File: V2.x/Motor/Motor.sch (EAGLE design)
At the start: 48 parts, among them IC1 Atmega 328-P, IC2 MCP2515, IC3 LM340MP-05, Q1 8MHz, Q2 16MHz

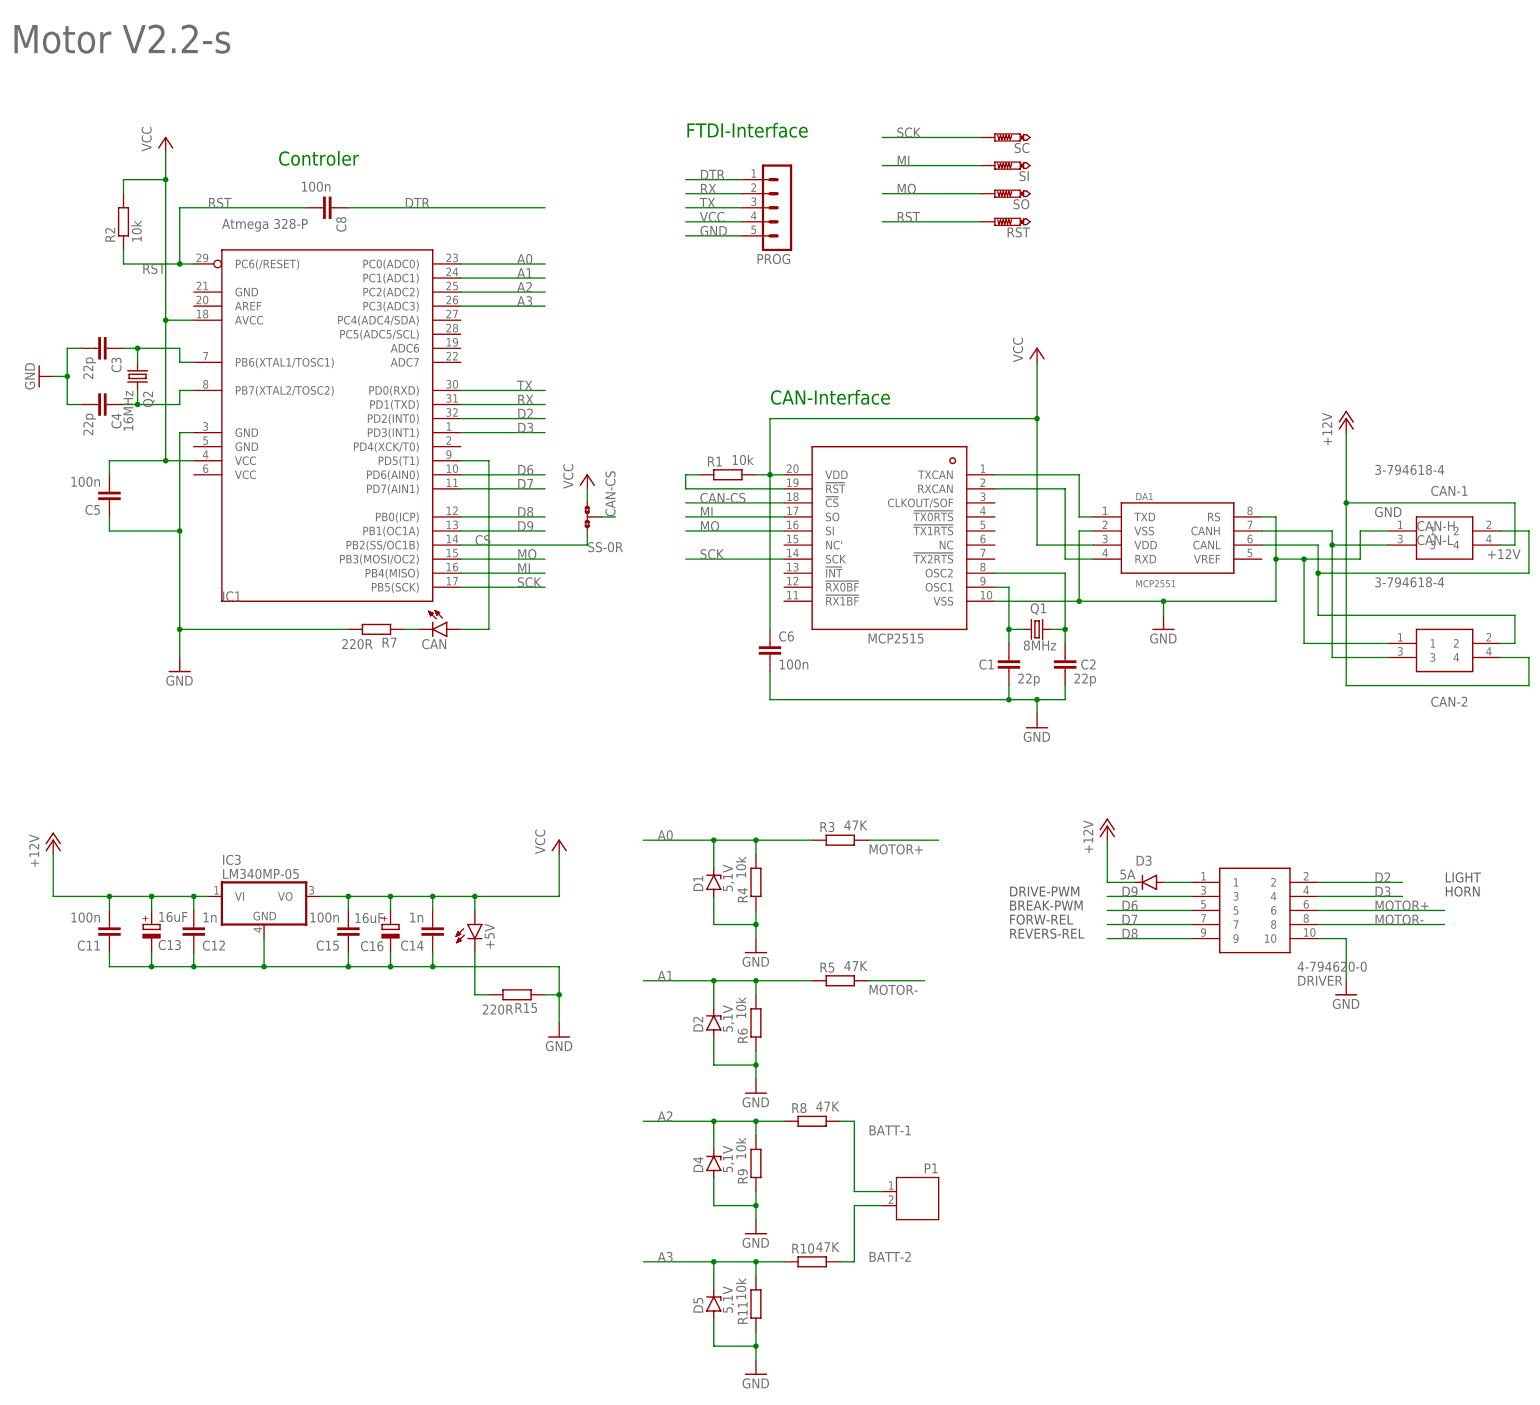
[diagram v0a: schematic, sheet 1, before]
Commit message: added Loco-CAN icon to motor, servo and switch boards
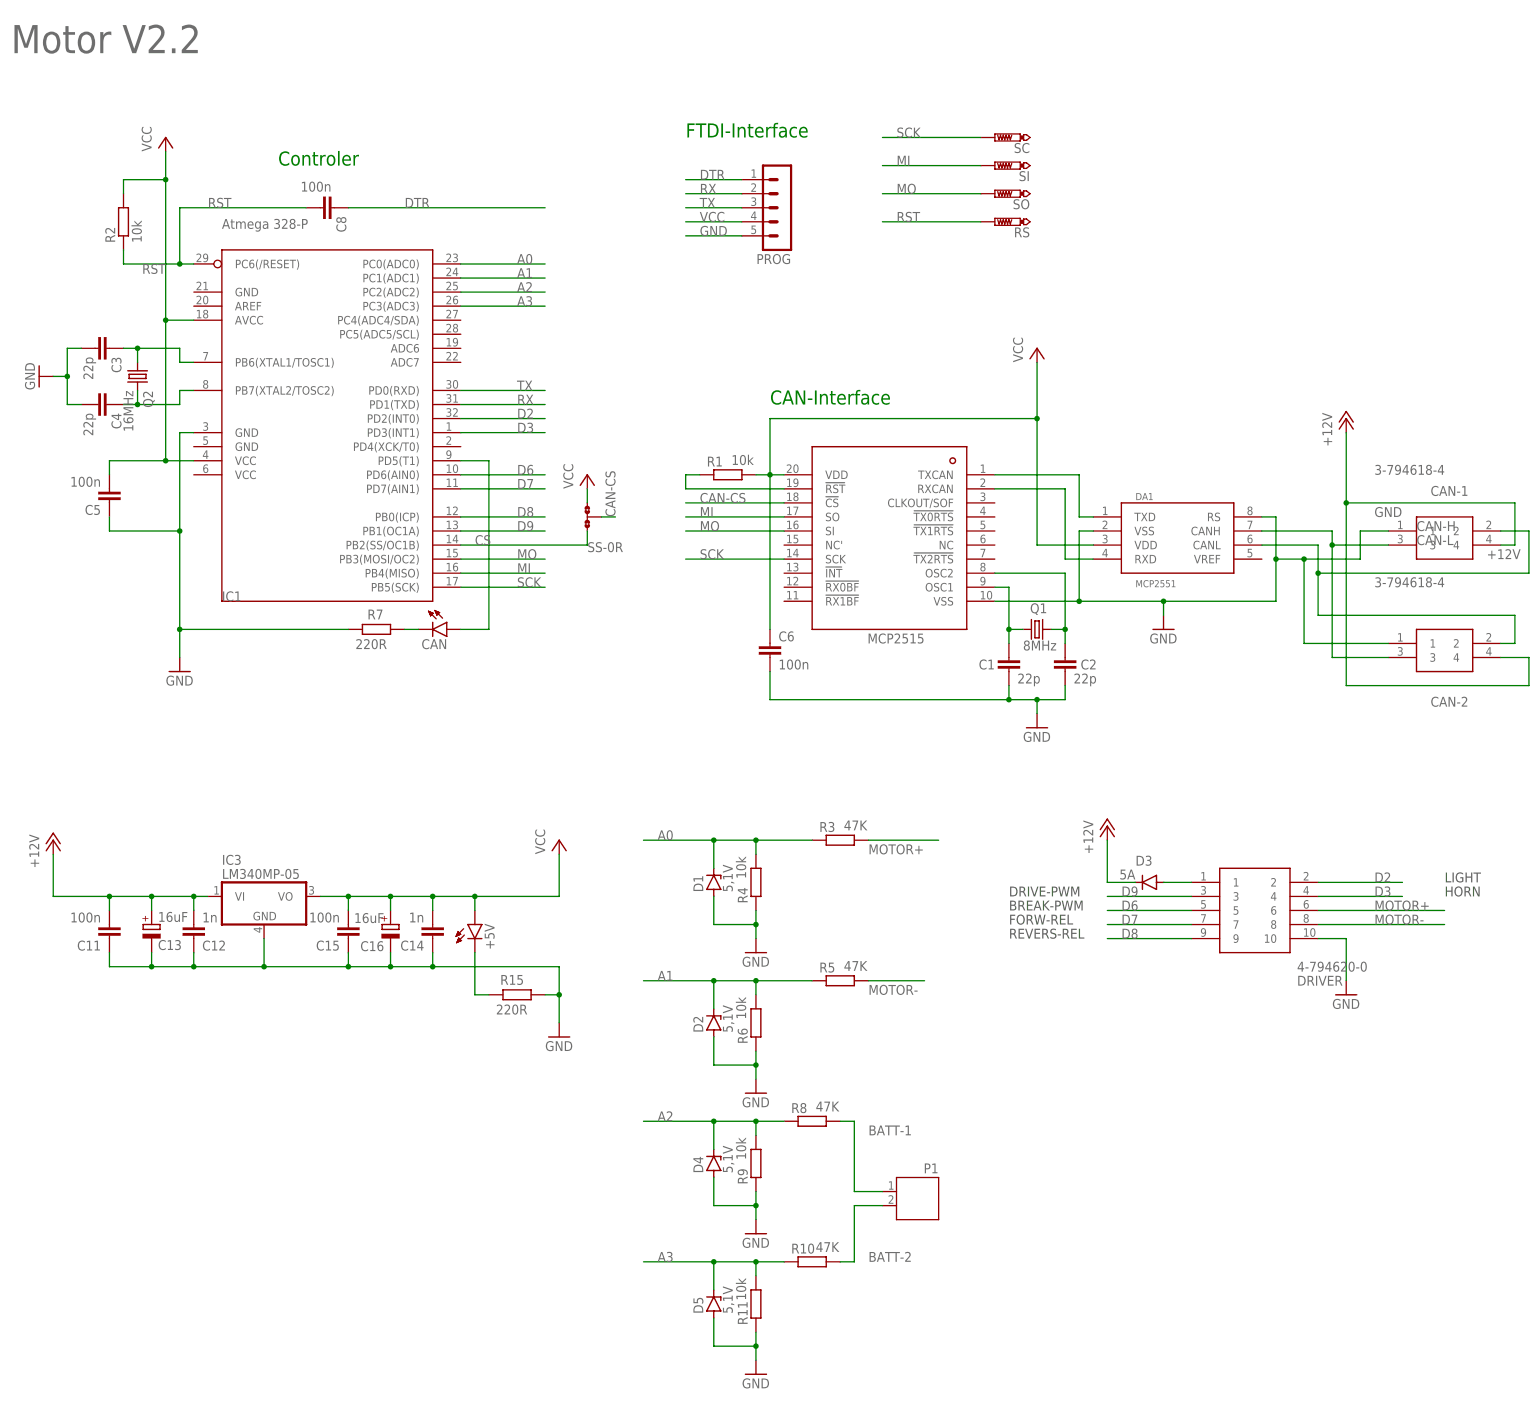
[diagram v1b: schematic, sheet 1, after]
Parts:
- renumbered RST to RS
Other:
- note added: "Motor V2.2"
- note removed: "Motor V2.2-s"
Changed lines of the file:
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@@
 <part name="SS" library="jump-0r-smd" library_urn="urn:adsk.eagle:library:251" deviceset="0R-JUMP" device="A" package3d_urn="urn:adsk.eagle:package:15385/1"/>
 <part name="P+5" library="supply1" library_urn="urn:adsk.eagle:library:371" deviceset="VCC" device=""/>
-<part name="RST" library="testpad" library_urn="urn:adsk.eagle:library:385" deviceset="PTR1" device="B1,27" package3d_urn="urn:adsk.eagle:package:27944/2"/>
+<part name="RS" library="testpad" library_urn="urn:adsk.eagle:library:385" deviceset="PTR1" device="B1,27" package3d_urn="urn:adsk.eagle:package:27944/2"/>
 <part name="R8" library="rcl" library_urn="urn:adsk.eagle:library:334" deviceset="R-EU_" device="MELF0102W" package3d_urn="urn:adsk.eagle:package:23588/2" value="47K"/>
 <part name="R9" library="rcl" library_urn="urn:adsk.eagle:library:334" deviceset="R-EU_" device="MELF0102W" package3d_urn="urn:adsk.eagle:package:23588/2" value="10k"/>
@@
 <text x="154.94" y="-48.26" size="1.778" layer="97" grouprefs="CONTROLER-PORT">REVERS-REL</text>
 <text x="233.68" y="-40.64" size="1.778" layer="97" grouprefs="CONTROLER-PORT">HORN</text>
-<text x="-25.4" y="111.76" size="5.08" layer="95">Motor V2.2-s</text>
+<text x="-25.4" y="111.76" size="5.08" layer="95">Motor V2.2</text>
 </plain>
 <instances>
@@
 </instance>
 <instance part="R15" gate="G$1" x="66.04" y="-58.42" smashed="yes" rot="R180" grouprefs="POWER">
-<attribute name="NAME" x="69.85" y="-59.9186" size="1.778" layer="95" rot="R180"/>
-<attribute name="VALUE" x="65.405" y="-60.198" size="1.778" layer="96" rot="R180"/>
+<attribute name="NAME" x="67.31" y="-54.8386" size="1.778" layer="95" rot="R180"/>
+<attribute name="VALUE" x="67.945" y="-60.198" size="1.778" layer="96" rot="R180"/>
 </instance>
 <instance part="+5V" gate="G$1" x="58.42" y="-45.72" smashed="yes" grouprefs="POWER">
@@
 </instance>
 <instance part="R7" gate="G$1" x="40.64" y="7.62" smashed="yes" rot="R180" grouprefs="MCU">
-<attribute name="NAME" x="44.45" y="6.1214" size="1.778" layer="95" rot="R180"/>
-<attribute name="VALUE" x="40.005" y="5.842" size="1.778" layer="96" rot="R180"/>
+<attribute name="NAME" x="41.91" y="11.2014" size="1.778" layer="95" rot="R180"/>
+<attribute name="VALUE" x="42.545" y="5.842" size="1.778" layer="96" rot="R180"/>
 </instance>
 <instance part="IC3" gate="A" x="20.32" y="-40.64" smashed="yes">
@@
 <attribute name="VALUE" x="76.2" y="33.02" size="1.778" layer="96" rot="R90"/>
 </instance>
-<instance part="RST" gate="G$1" x="152.4" y="81.28" smashed="yes" rot="R90" grouprefs="ICP">
+<instance part="RS" gate="G$1" x="152.4" y="81.28" smashed="yes" rot="R90" grouprefs="ICP">
 <attribute name="NAME" x="158.75" y="80.264" size="1.778" layer="95" rot="R180"/>
 <attribute name="TP_SIGNAL_NAME" x="154.94" y="82.55" size="1.778" layer="97" rot="R90"/>
@@
 <segment>
 <wire x1="132.08" y1="81.28" x2="149.86" y2="81.28" width="0.1524" layer="91" grouprefs="ICP"/>
-<pinref part="RST" gate="G$1" pin="TP"/>
+<pinref part="RS" gate="G$1" pin="TP"/>
 <label x="134.62" y="81.28" size="1.778" layer="95" grouprefs="ICP"/>
 </segment>
